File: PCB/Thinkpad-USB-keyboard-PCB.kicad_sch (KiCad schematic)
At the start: 71 parts, among them J1 TYPE-C-31-M12_13, J2 USB_A, J3 USB_A, J4 TYPE-C-31-M12_13, J6 TYPE-C-31-M12_13, U1 USBLC6-2SC6, U2 RP2040, U3 USB2514B_Bi, U4 USBLC6-2SC6, U5 USBLC6-2SC6, U7 USBLC6-2SC6, U8 TLV1117-33, Y1 Crystal_GND24

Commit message: More work
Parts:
- removed J1, J6: TYPE-C-31-M12_13, AcheronConnectors:TYPE-C-31-M-12, symbol AcheronLib:TYPE-C-31-M12_13
- added C26: 100nF, Capacitor_SMD:C_0402_1005Metric, symbol Device:C_Small
- added J1, J7: USB_C_Receptacle_USB2.0, Connector_USB:USB_C_Receptacle_HRO_TYPE-C-31-M-12, symbol Connector:USB_C_Receptacle_USB2.0
- added J5: Conn_02x20_Odd_Even, symbol Connector_Generic:Conn_02x20_Odd_Even
- added R15, R16: 1k, Resistor_SMD:R_0805_2012Metric_Pad1.15x1.40mm_HandSolder, symbol Device:R_Small
- added SW1, SW2: SW_Push, Button_Switch_THT:SW_PUSH_6mm_H5mm, symbol Switch:SW_Push
- added SW3: SW_Push, Connector_PinSocket_2.54mm:PinSocket_1x02_P2.54mm_Vertical, symbol Switch:SW_Push
- added U6: W25Q128JVS, Package_SO:SOIC-8_5.23x5.23mm_P1.27mm, symbol Memory_Flash:W25Q128JVS
- added Y2: Crystal_GND24, Crystal:Crystal_SMD_3225-4Pin_3.2x2.5mm_HandSoldering, symbol Device:Crystal_GND24
- C5, C9: value 15pF -> 22pF
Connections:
- net +3V3: now also C26.1, R16.2, U6.8 (VCC)
- net D2+: now also J7.A6 (D+), J7.B6 (D+)
- net D2-: now also J7.A7 (D-), J7.B7 (D-)
- net DUP+: now also J1.A6 (D+), J1.B6 (D+)
- net DUP-: now also J1.A7 (D-), J1.B7 (D-)
- net GND: now also C5.1, C9.1, R1.2, R2.2, C26.2, J1.A1 (GND), J1.A12 (GND), J1.B1 (GND), J1.B12 (GND), J7.A1 (GND), J7.A12 (GND), J7.B1 (GND), J7.B12 (GND), SW3.1, U6.4 (GND), Y2.2, Y2.4
- net GNDPWR: now also J1.S1 (SHIELD), J7.S1 (SHIELD); no longer R1.2, R2.2
- net VBUS: now also J1.A4 (VBUS), J1.A9 (VBUS), J1.B4 (VBUS), J1.B9 (VBUS), J7.A4 (VBUS), J7.A9 (VBUS), J7.B4 (VBUS), J7.B9 (VBUS)
- net at R8.1: now also J7.A5 (CC1)
- net at R9.1: now also J7.B5 (CC2)
- net at C9.2: now also R14.1, Y2.3
- net at R1.1: now also J1.A5 (CC1)
- net at R2.1: now also J1.B5 (CC2)
- net at U2.20 (XIN): now also C5.2, Y2.1
- net RESET: now reaches U2.26 (RUN)
- net RESET: now also R16.1
- net SD3: now reaches U2.51 (QSPI_SD3)
- net SD3: now also U6.7 (IO3)
- net QSPI_CLK: now reaches U2.52 (QSPI_SCLK)
- net QSPI_CLK: now also U6.6 (CLK)
- net SD0: now reaches U2.53 (QSPI_SD0)
- net SD0: now also U6.5 (DI(IO0))
- net SD2: now reaches U2.54 (QSPI_SD2)
- net SD2: now also U6.3 (IO2)
- net SD1: now reaches U2.55 (QSPI_SD1)
- net SD1: now also U6.2 (DO(IO1))
- net CS: now reaches U2.56 (QSPI_SS)
- net CS: now also R15.2, U6.1 (~{CS})
- new net ~{USB_BOOT}: R15.1, SW3.2
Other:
- note added: "BOOT"
- note added: "RESET"
- moved on the sheet: C5, C9, L1, L2, R1, R2, R8, R9

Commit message: More work
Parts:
- removed C21: 10u, Capacitor_SMD:C_0805_2012Metric_Pad1.15x1.40mm_HandSolder, symbol Device:C
- removed J4: TYPE-C-31-M12_13, AcheronConnectors:TYPE-C-31-M-12, symbol AcheronLib:TYPE-C-31-M12_13
- removed J5: Conn_02x20_Odd_Even, symbol Connector_Generic:Conn_02x20_Odd_Even
- removed L3: 60R@100MHz, Inductor_SMD:L_1206_3216Metric, symbol Unified-Daughterboard-rescue:L_Core_Ferrite-Device
- removed R11: 56k, Resistor_SMD:R_0805_2012Metric_Pad1.15x1.40mm_HandSolder, symbol Device:R_Small
- removed R4: 1M, Resistor_SMD:R_0805_2012Metric_Pad1.15x1.40mm_HandSolder, symbol Device:R
- removed SW2: SW_Push, Button_Switch_THT:SW_PUSH_6mm_H5mm, symbol Switch:SW_Push
- removed U1, U4, U5, U7: USBLC6-2SC6, Package_TO_SOT_SMD:SOT-23-6, symbol Power_Protection:USBLC6-2SC6
- added C21: 1uF, Capacitor_SMD:C_0402_1005Metric, symbol Device:C_Small
- added C27, C28: 100nF, Capacitor_SMD:C_0402_1005Metric, symbol Device:C_Small
- added J4: SWD, Connector_PinSocket_2.54mm:PinSocket_1x05_P2.54mm_Vertical, symbol Connector_Generic:Conn_01x05
- added J6: Conn_02x20_Odd_Even_MountingPin, A-Thinkpad-USB-keyboard-footprints:Molex Slimstack 54363-0489, symbol Connector_Generic_MountingPin:Conn_02x20_Odd_Even_MountingPin
- added R17, R18: 4.7K, Resistor_SMD:R_0805_2012Metric_Pad1.15x1.40mm_HandSolder, symbol Device:R_Small
- added R19: 10k, Resistor_SMD:R_0805_2012Metric_Pad1.15x1.40mm_HandSolder, symbol Device:R_Small
- added U1, U10, U4, U5: SRV05-4, Package_TO_SOT_SMD:SOT-23-6, symbol Power_Protection:SRV05-4
- R10: value 56k -> 100; LCSC (none) -> C11702; Package R0603 -> (none)
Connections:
- net D1P+ is gone; now on net D1+: U3.2 (USBDP_DN1/PRT_DIS_P1)
- net D1P- is gone; now on net D1-: U3.1 (USBDM_DN1/PRT_DIS_M1)
- net D2P+ is gone; now on net D2+: U3.4 (USBDP_DN2/PRT_DIS_P2)
- net D2P- is gone; now on net D2-: U3.3 (USBDM_DN2/PRT_DIS_M2)
- net D4P+ is gone; now on net D4+: U3.9 (USBDP_DN4/PRT_DIS_P4)
- net D4P- is gone; now on net D4-: U3.8 (USBDM_DN4/PRT_DIS_M4)
- net DUPP+ is gone; now on net DUP+: U3.31 (USBDP_UP)
- net DUPP- is gone; now on net DUP-: U3.30 (USBDM_UP)
- net VCC is gone; now on net +5V: C18.1, C19.1, C20.1, D1.2 (A2), F1.2, J2.1 (VBUS), J3.1 (VBUS)
- net +1V1: now also C21.1, C27.1, C28.1
- net +3V3: now also R10.2, SW1.2, J4.2 (Pin_2), J6.35 (Pin_35), R17.2, R18.2, R19.2
- net +5V: now also J7.A4 (VBUS), J7.A9 (VBUS), J7.B4 (VBUS), J7.B9 (VBUS), R8.2, R9.2, J6.38 (Pin_38), U1.5 (VP), U4.5 (VP), U5.5 (VP)
- net D1+: now also U1.1 (IO1)
- net D1-: now also U1.3 (IO2)
- net D2+: now also R3.1; no longer J7.A6 (D+), J7.B6 (D+)
- net D2-: now also R13.1; no longer J7.A7 (D-), J7.B7 (D-)
- net D3+: now also J7.A6 (D+), J7.B6 (D+), U4.6 (IO4); no longer R3.1
- net D3-: now also J7.A7 (D-), J7.B7 (D-), U4.4 (IO3); no longer R13.1
- net D4+: now also U5.6 (IO4)
- net D4-: now also U5.4 (IO3)
- net DUP+: now also U10.3 (IO2)
- net DUP-: now also U10.1 (IO1)
- net GND: now also SW1.1, C21.2, C27.2, C28.2, J4.3 (Pin_3), J6.31 (Pin_31), J6.34 (Pin_34), J6.MP (MountPin), U1.2 (VN), U10.2 (VN), U4.2 (VN), U5.2 (VN)
- net VBUS: now also U10.5 (VP); no longer J7.A4 (VBUS), J7.A9 (VBUS), J7.B4 (VBUS), J7.B9 (VBUS), R10.2, R8.2, R9.2
- net at C9.2, R14.1: now also Y2.1; no longer Y2.3
- net at C5.2, U2.20 (XIN): now also Y2.3; no longer Y2.1
- net LED-CAPS-LOCK: now reaches R10.1
- net LED-CAPS-LOCK: now also U2.37 (GPIO25), J6.21 (Pin_21)
- net SENSE6: now reaches U2.11 (GPIO8)
- net SENSE6: now also J6.15 (Pin_15)
- net TP4-DATA: now reaches U2.13 (GPIO10)
- net TP4-DATA: now also J6.37 (Pin_37), R18.1
- net LED-MIC-MUTE: now reaches U2.15 (GPIO12)
- net LED-MIC-MUTE: now also J6.36 (Pin_36)
- net DRV13: now reaches U2.16 (GPIO13)
- net DRV13: now also J6.32 (Pin_32)
- net DRV15: now reaches U2.17 (GPIO14)
- net DRV15: now also J6.30 (Pin_30)
- net DRV12: now reaches U2.18 (GPIO15)
- net DRV12: now also J6.28 (Pin_28)
- net DRV4: now reaches U2.2 (GPIO0)
- net DRV4: now also J6.2 (Pin_2)
- net SWCLK: now reaches U2.24 (SWCLK)
- net SWCLK: now also J4.5 (Pin_5)
- net SWD: now reaches U2.25 (SWD)
- net SWD: now also J4.4 (Pin_4)
- net DRV14: now reaches U2.27 (GPIO16)
- net DRV14: now also J6.26 (Pin_26)
- net DRV11: now reaches U2.28 (GPIO17)
- net DRV11: now also J6.24 (Pin_24)
- net SENSE1: now reaches U2.29 (GPIO18)
- net SENSE1: now also J6.13 (Pin_13)
- net DRV5: now reaches U2.3 (GPIO1)
- net DRV5: now also J6.4 (Pin_4)
- net SENSE4: now reaches U2.30 (GPIO19)
- net SENSE4: now also J6.11 (Pin_11)
- net SENSE2: now reaches U2.31 (GPIO20)
- net SENSE2: now also J6.9 (Pin_9)
- net SENSE3: now reaches U2.32 (GPIO21)
- net SENSE3: now also J6.7 (Pin_7)
- net SENSE0: now reaches U2.34 (GPIO22)
- net SENSE0: now also J6.5 (Pin_5)
- net SENSE5: now reaches U2.35 (GPIO23)
- net SENSE5: now also J6.3 (Pin_3)
- net HOTKEY: now reaches U2.36 (GPIO24)
- net HOTKEY: now also J6.1 (Pin_1)
- net DRV9: now reaches U2.38 (GPIO26_ADC0)
- net DRV9: now also J6.20 (Pin_20)
- net DRV0: now reaches U2.39 (GPIO27_ADC1)
- net DRV0: now also J6.22 (Pin_22)
- net DRV8: now reaches U2.4 (GPIO2)
- net DRV8: now also J6.6 (Pin_6)
- net DRV1: now reaches U2.40 (GPIO28_ADC2)
- net DRV1: now also J6.18 (Pin_18)
- net DRV6: now reaches U2.5 (GPIO3)
- net DRV6: now also J6.8 (Pin_8)
- net DRV3: now reaches U2.6 (GPIO4)
- net DRV3: now also J6.10 (Pin_10)
- net DRV7: now reaches U2.7 (GPIO5)
- net DRV7: now also J6.12 (Pin_12)
- net DRV2: now reaches U2.8 (GPIO6)
- net DRV2: now also J6.14 (Pin_14)
- net DRV10: now reaches U2.9 (GPIO7)
- net DRV10: now also J6.16 (Pin_16)
- net PS2-CLK renamed TP4-CLK
- net TP4-CLK: now also J6.39 (Pin_39), R17.1
- net PS2-DATA renamed SENSE7
- net SENSE7: now also J6.17 (Pin_17)
- new net LED-POWER: J6.23 (Pin_23)
- new net PWRSWITCH: J6.19 (Pin_19)
- new net TP4-RESET: J6.40 (Pin_40), R19.1
- new net ~{RESET}: J4.1 (Pin_1)
- no-connect marks 17 -> 15
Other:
- note removed: "BOOT"
- moved on the sheet: H10, H11, H12, H5, H6, H7, H8, H9, J3, SW1, Y2

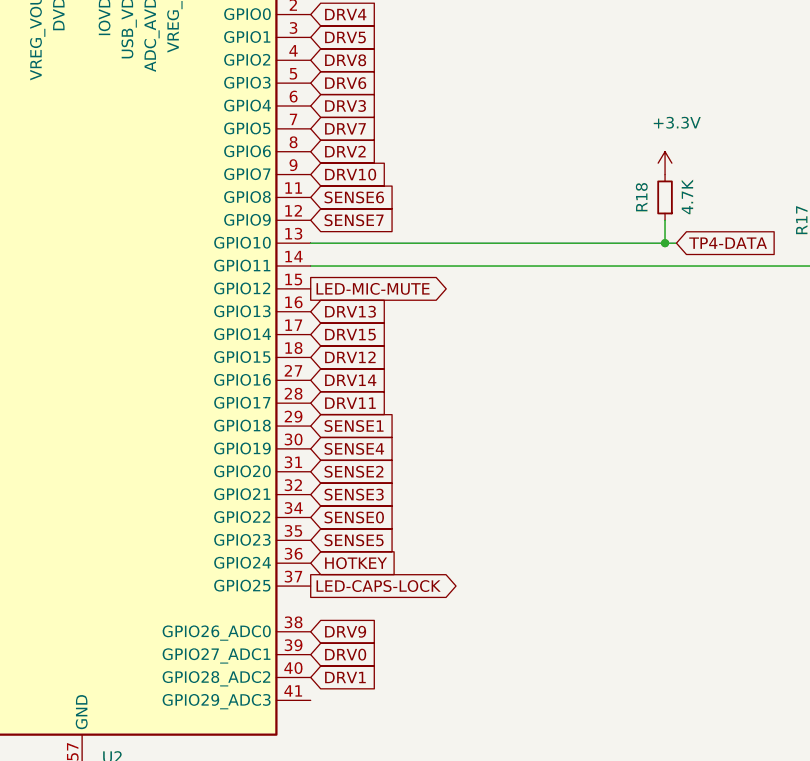
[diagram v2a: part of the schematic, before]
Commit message: Made a breakout board for the Thinkpad keyboard connector
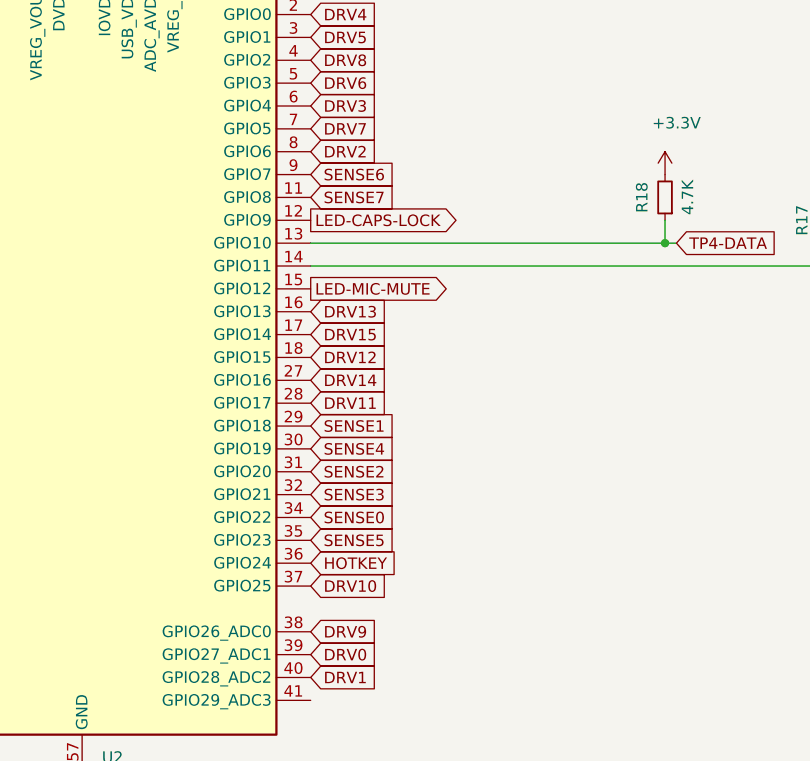
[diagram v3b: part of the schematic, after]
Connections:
- net DRV10: now also U2.37 (GPIO25); no longer U2.9 (GPIO7)
- net LED-CAPS-LOCK: now also U2.12 (GPIO9); no longer U2.37 (GPIO25)
- net SENSE6: now also U2.9 (GPIO7); no longer U2.11 (GPIO8)
- net SENSE7: now also U2.11 (GPIO8); no longer U2.12 (GPIO9)

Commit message: More work
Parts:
- removed C21: 1uF, Capacitor_SMD:C_0402_1005Metric, symbol Device:C_Small
- removed H1, H10, H2, H3, H9: MountingHole, MountingHole:MountingHole_3.2mm_M3_ISO7380, symbol Mechanical:MountingHole
- removed H11, H12, H6, H7, H8: MountingHole, MountingHole:MountingHole_2.2mm_M2_ISO7380, symbol Mechanical:MountingHole
- added C21, C29: 1uF, Capacitor_SMD:C_0603_1608Metric_Pad1.08x0.95mm_HandSolder, symbol Device:C
- added C30, C31: 100nF, Capacitor_SMD:C_0402_1005Metric_Pad0.74x0.62mm_HandSolder, symbol Device:C
- added H2, H3, H4, H6, H7, H8: MountingHole_Pad, MountingHole:MountingHole_3.2mm_M3_ISO7380_Pad, symbol Mechanical:MountingHole_Pad
- C1, C18, C19, C2, C20, C25: value 10u -> 10uF; footprint Capacitor_SMD:C_0805_2012Metric_Pad1.15x1.40mm_HandSolder -> Capacitor_SMD:C_1206_3216Metric_Pad1.33x1.80mm_HandSolder
- C10, C11, C12, C13, C22, C23, C24, C3, C4, C6, C7, C8: footprint Capacitor_SMD:C_0603_1608Metric_Pad1.05x0.95mm_HandSolder -> Capacitor_SMD:C_0402_1005Metric_Pad0.74x0.62mm_HandSolder
- C14, C15, C16, C17: footprint Capacitor_SMD:C_1206_3216Metric_Pad1.42x1.75mm_HandSolder -> Capacitor_SMD:C_1206_3216Metric_Pad1.33x1.80mm_HandSolder
- C26, C27, C28: footprint Capacitor_SMD:C_0402_1005Metric -> Capacitor_SMD:C_0402_1005Metric_Pad0.74x0.62mm_HandSolder
- C5, C9: footprint (none) -> Capacitor_SMD:C_0402_1005Metric_Pad0.74x0.62mm_HandSolder
- D1: footprint AcheronComponents:D_SOD-123_Bidirectional -> Diode_SMD:D_SOD-123
- D3, D4: footprint acheronComponents:D_SOD-123 -> Diode_SMD:D_SOD-123
- H5: footprint MountingHole:MountingHole_2.2mm_M2_ISO7380_Pad -> MountingHole:MountingHole_3.2mm_M3_ISO7380_Pad
- R1, R10, R14, R15, R16, R17, R18, R19, R2, R5, R6, R7, R8, R9: footprint Resistor_SMD:R_0805_2012Metric_Pad1.15x1.40mm_HandSolder -> Resistor_SMD:R_0805_2012Metric_Pad1.20x1.40mm_HandSolder
- R13, R3: footprint Resistor_SMD:R_0805_2012Metric_Pad1.15x1.40mm_HandSolder -> Capacitor_SMD:C_0402_1005Metric_Pad0.74x0.62mm_HandSolder
- renumbered H4 to H1
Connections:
- net +1V1: now also C21.1
- net +3V3: now also C29.1, C30.1, C31.1
- net DRV0: now also U2.28 (GPIO17); no longer U2.39 (GPIO27_ADC1)
- net DRV1: now also U2.30 (GPIO19); no longer U2.40 (GPIO28_ADC2)
- net DRV10: now also U2.31 (GPIO20); no longer U2.37 (GPIO25)
- net DRV11: now also U2.27 (GPIO16); no longer U2.28 (GPIO17)
- net DRV12: now also U2.17 (GPIO14); no longer U2.18 (GPIO15)
- net DRV13: now also U2.15 (GPIO12); no longer U2.16 (GPIO13)
- net DRV14: now also U2.18 (GPIO15); no longer U2.27 (GPIO16)
- net DRV15: now also U2.16 (GPIO13); no longer U2.17 (GPIO14)
- net DRV2: now also U2.32 (GPIO21); no longer U2.8 (GPIO6)
- net DRV3: now also U2.35 (GPIO23); no longer U2.6 (GPIO4)
- net DRV4: now also U2.39 (GPIO27_ADC1); no longer U2.2 (GPIO0)
- net DRV5: now also U2.38 (GPIO26_ADC0); no longer U2.3 (GPIO1)
- net DRV6: now also U2.36 (GPIO24); no longer U2.5 (GPIO3)
- net DRV7: now also U2.34 (GPIO22); no longer U2.7 (GPIO5)
- net DRV8: now also U2.37 (GPIO25); no longer U2.4 (GPIO2)
- net DRV9: now also U2.29 (GPIO18); no longer U2.38 (GPIO26_ADC0)
- net GND: now also C21.2, C29.2, C30.2, C31.2
- net GNDPWR: now also H2.1, H3.1, H4.1, H6.1, H7.1, H8.1
- net HOTKEY: now also U2.40 (GPIO28_ADC2); no longer U2.36 (GPIO24)
- net LED-MIC-MUTE: no longer U2.15 (GPIO12)
- net PWRSWITCH: now also U2.11 (GPIO8)
- net SENSE0: now also U2.3 (GPIO1); no longer U2.34 (GPIO22)
- net SENSE1: now also U2.7 (GPIO5); no longer U2.29 (GPIO18)
- net SENSE2: now also U2.5 (GPIO3); no longer U2.31 (GPIO20)
- net SENSE3: now also U2.4 (GPIO2); no longer U2.32 (GPIO21)
- net SENSE4: now also U2.6 (GPIO4); no longer U2.30 (GPIO19)
- net SENSE5: now also U2.2 (GPIO0); no longer U2.35 (GPIO23)
- net SENSE6: now also U2.8 (GPIO6); no longer U2.9 (GPIO7)
- net SENSE7: now also U2.9 (GPIO7); no longer U2.11 (GPIO8)
- net KBDID0: now reaches J6.25 (Pin_25)
- net KBDID1: now reaches J6.27 (Pin_27)
- net KBDID2: now reaches J6.29 (Pin_29)
- net LED-VOL-MUTE: now reaches J6.33 (Pin_33)
- net TP4-RESET-3V3: now reaches U2.41 (GPIO29_ADC3)
- net TP4-CLK renamed TP4-CLK-3V3
- net TP4-CLK-3V3: no longer J6.39 (Pin_39)
- net TP4-DATA renamed TP4-DATA-3V3
- net TP4-DATA-3V3: no longer J6.37 (Pin_37)
- net TP4-RESET renamed TP4-RESET-5V
- new net TP4-CLK-5V: J6.39 (Pin_39)
- new net TP4-DATA-5V: J6.37 (Pin_37)
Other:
- added sheet BSS138 Level Shifter (BSS138-level-shifter.kicad_sch)
- added sheet BSS138 Level Shifter1 (BSS138-level-shifter.kicad_sch)
- added sheet BSS138 Level Shifter2 (BSS138-level-shifter.kicad_sch)
- note added: "Level shifting"
- note added: "Mounting Holes"
- moved on the sheet: C11, C22, C23, C24, C26, H1, R15, R18, SW3, U6
